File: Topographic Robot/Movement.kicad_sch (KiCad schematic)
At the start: 26 parts, among them M1 MG946R, M10 MG946R, M11 MG946R, M12 MG946R, M13 MG946R, M14 MG946R, M15 MG946R, M16 MG946R, M17 MG946R, M18 MG946R, M19 SG90, M2 MG946R, M20 SG90, M21 SG90, M22 SG90, M23 SG90, M24 SG90, M3 MG946R, M4 MG946R, M5 MG946R, M6 MG946R, M7 MG946R, M8 MG946R, M9 MG946R, U15 PCA9685, U16 PCA9685

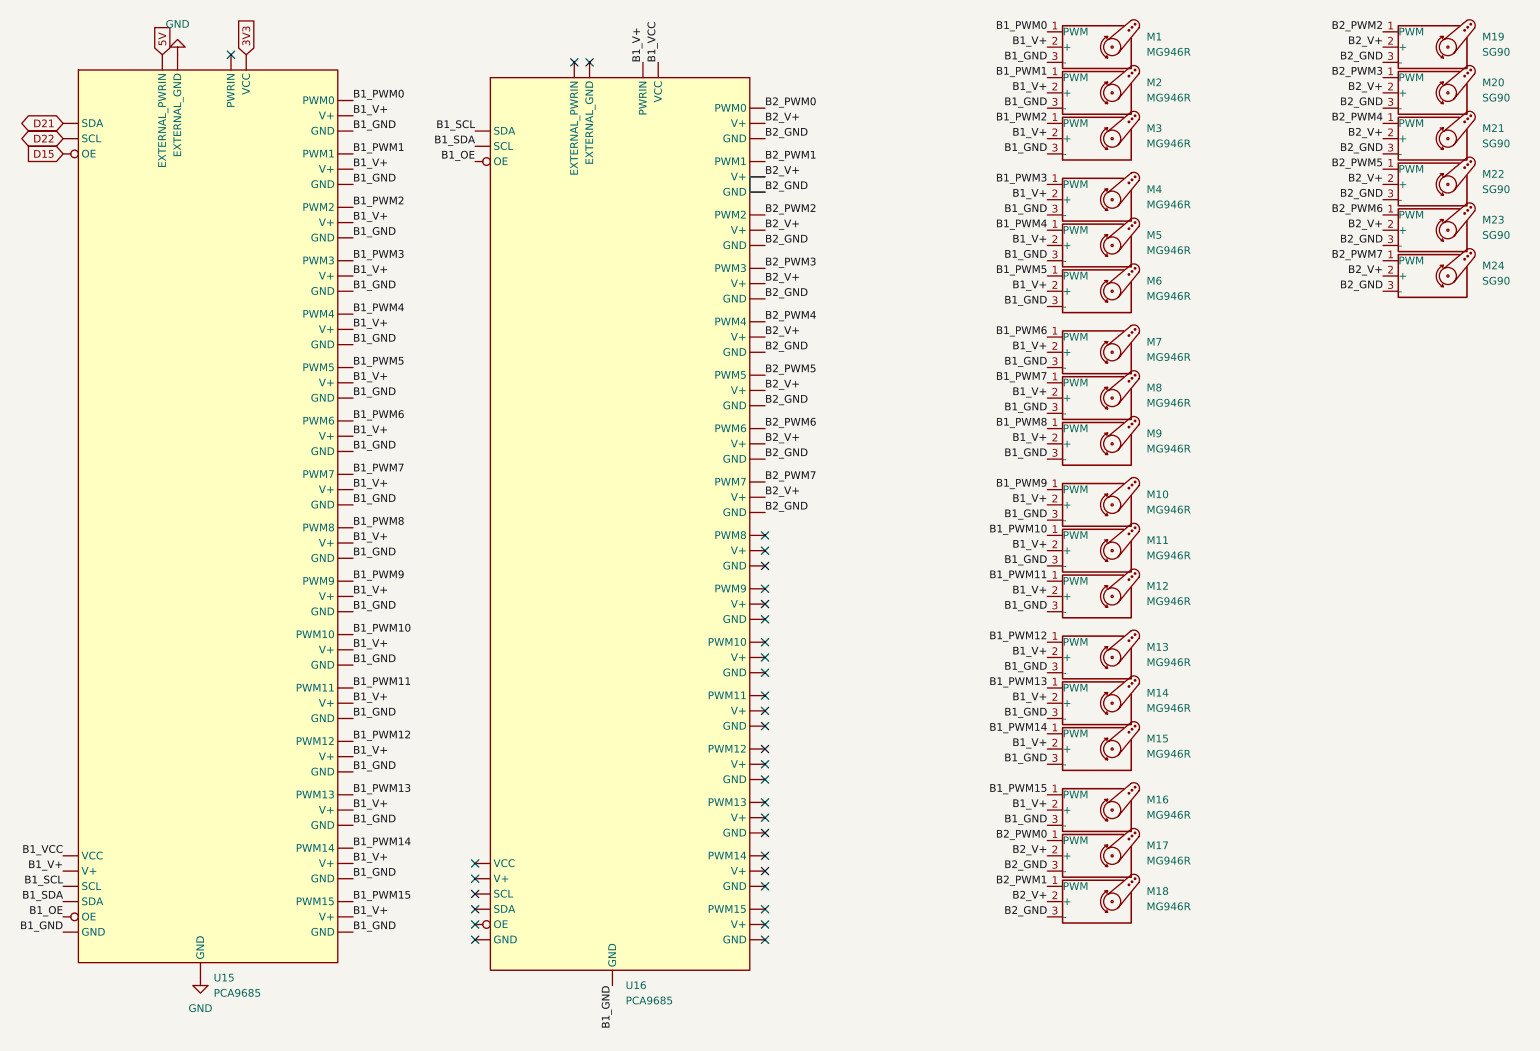
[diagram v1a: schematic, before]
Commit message: Parallel > USB ?!
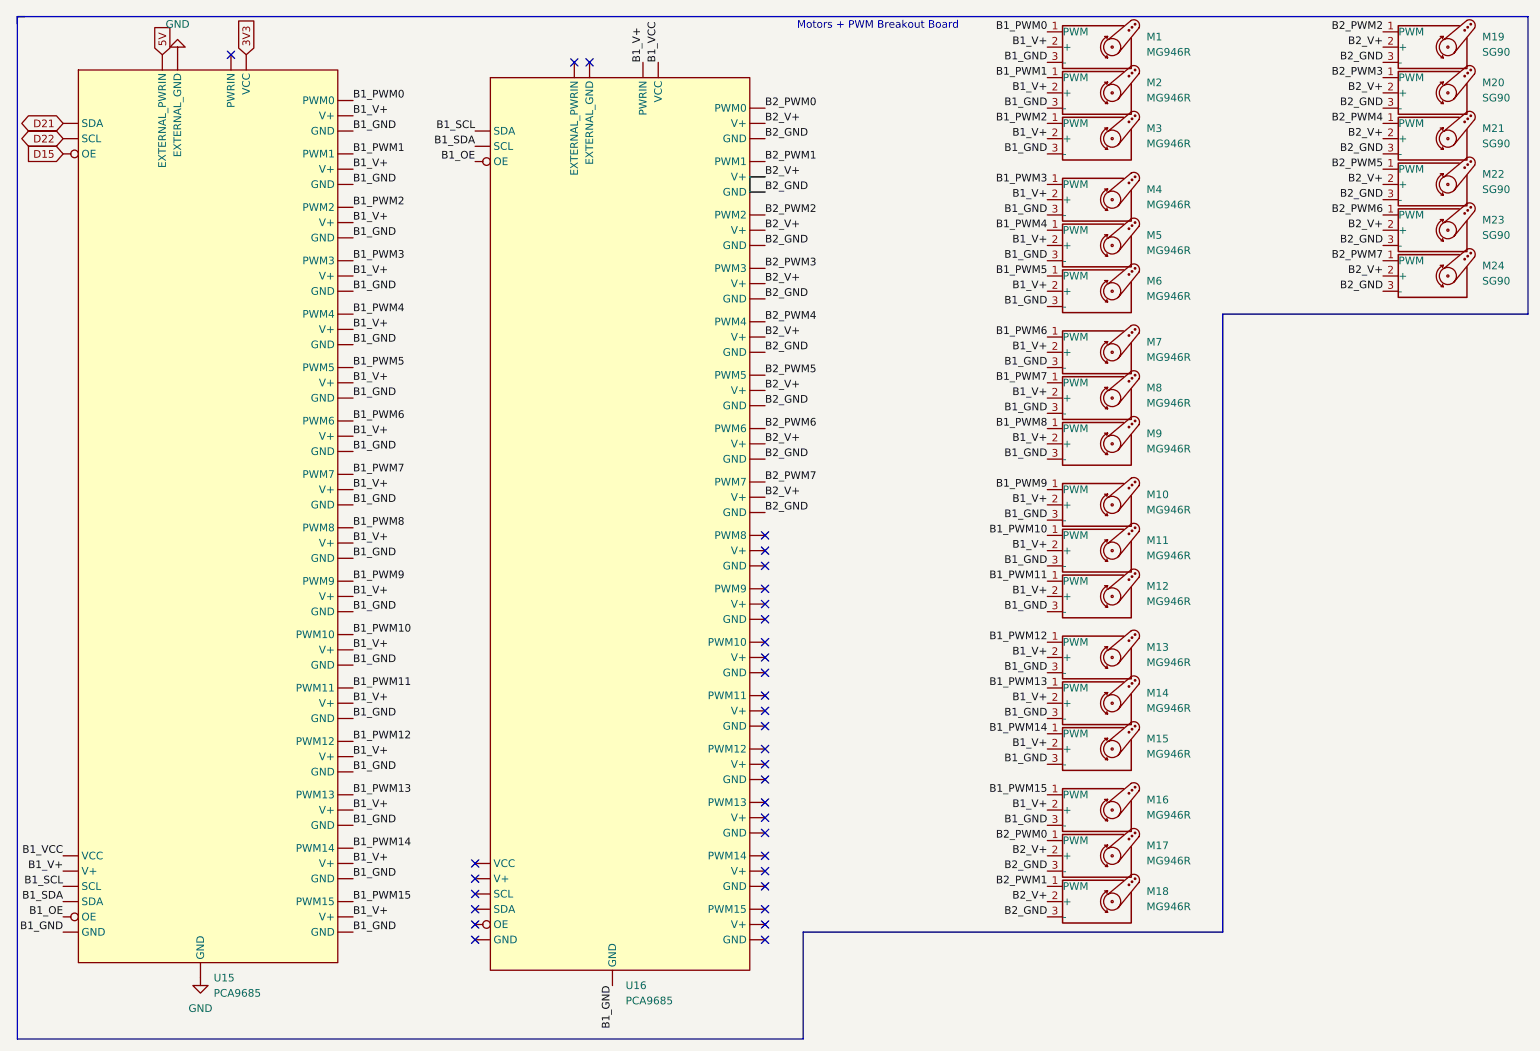
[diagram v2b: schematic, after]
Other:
- note added: "Motors + PWM Breakout Board"
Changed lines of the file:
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@@
+		)
+	)
+	(polyline
+		(pts
+			(xy 12.7 12.7) (xy 12.7 13.97)
+		)
+		(stroke
+			(width 0)
+			(type default)
+		)
+	)
+	(polyline
+		(pts
+			(xy 143.51 182.88) (xy 12.7 182.88)
+		)
+		(stroke
+			(width 0)
+			(type default)
 		)
 	)
@@
 		(pts
 			(xy 137.16 39.37) (xy 134.62 39.37)
+		)
+		(stroke
+			(width 0)
+			(type default)
+		)
+	)
+	(polyline
+		(pts
+			(xy 12.7 12.7) (xy 13.97 12.7)
+		)
+		(stroke
+			(width 0)
+			(type default)
+		)
+	)
+	(polyline
+		(pts
+			(xy 12.7 12.7) (xy 264.16 12.7)
+		)
+		(stroke
+			(width 0)
+			(type default)
+		)
+	)
+	(polyline
+		(pts
+			(xy 213.36 165.1) (xy 143.51 165.1)
+		)
+		(stroke
+			(width 0)
+			(type default)
+		)
+	)
+	(polyline
+		(pts
+			(xy 12.7 182.88) (xy 12.7 12.7)
+		)
+		(stroke
+			(width 0)
+			(type default)
+		)
+	)
+	(polyline
+		(pts
+			(xy 213.36 62.23) (xy 213.36 165.1)
 		)
 		(stroke
@@
 		)
 	)
+	(polyline
+		(pts
+			(xy 264.16 62.23) (xy 213.36 62.23)
+		)
+		(stroke
+			(width 0)
+			(type default)
+		)
+	)
+	(polyline
+		(pts
+			(xy 143.51 165.1) (xy 143.51 182.88)
+		)
+		(stroke
+			(width 0)
+			(type default)
+		)
+	)
+	(polyline
+		(pts
+			(xy 264.16 12.7) (xy 264.16 62.23)
+		)
+		(stroke
+			(width 0)
+			(type default)
+		)
+	)
+	(text "Motors + PWM Breakout Board"
+		(exclude_from_sim no)
+		(at 155.956 14.224 0)
+		(effects
+			(font
+				(size 1.27 1.27)
+			)
+		)
+	)
